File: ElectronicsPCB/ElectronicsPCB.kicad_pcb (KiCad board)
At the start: 4 copper layers, 15 parts

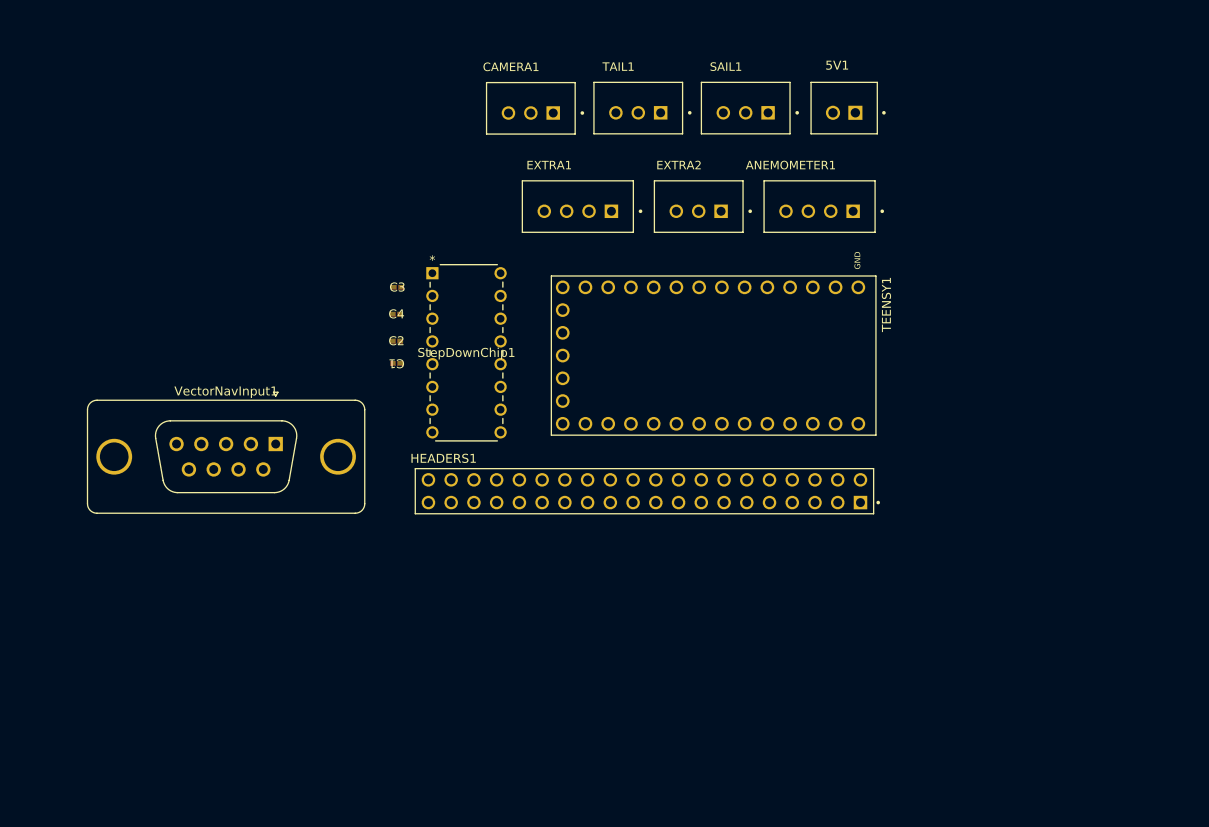
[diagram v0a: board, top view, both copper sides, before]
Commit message: added xbee footprint & xbee to layout
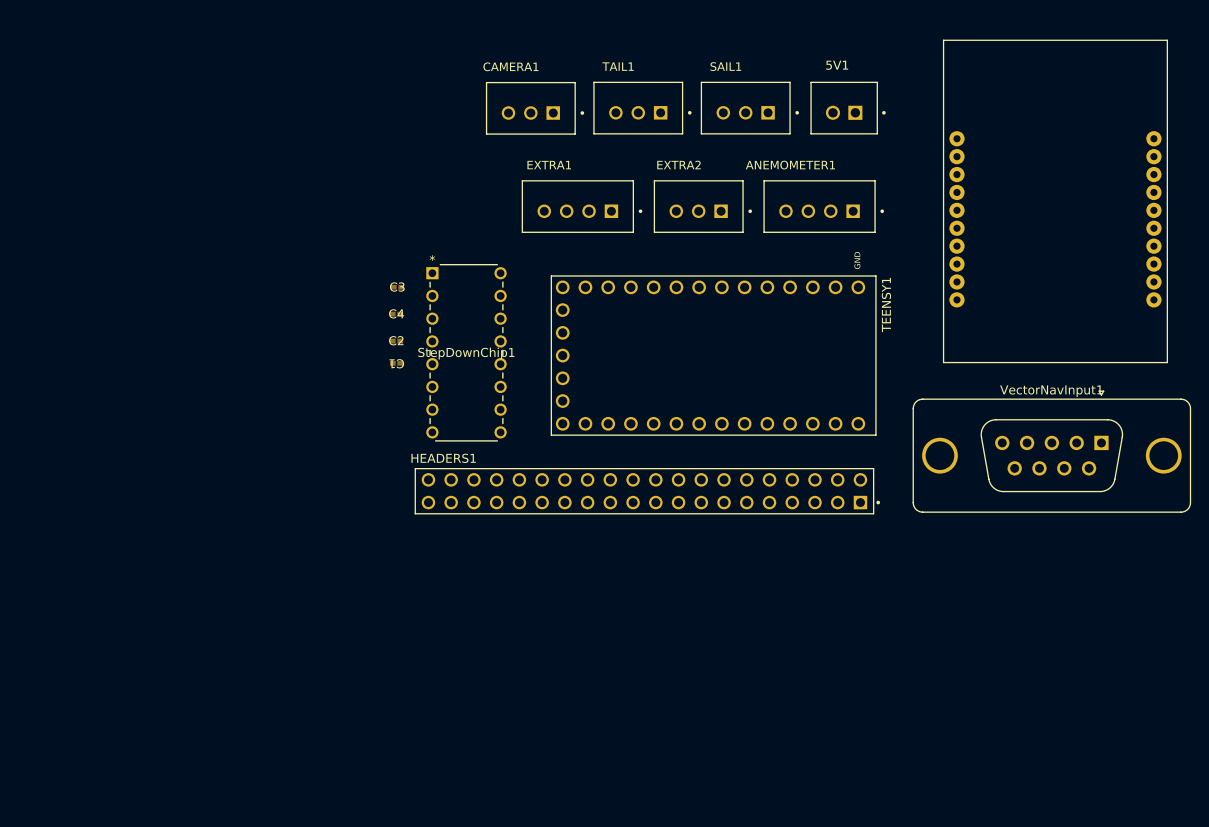
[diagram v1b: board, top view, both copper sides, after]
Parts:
- added XBEE1: ~, ElectronicsFootprints:XBee, F.Cu at (211.6, 66.9)
- moved VectorNavInput1 92.2 mm to (214.2, 95.9)

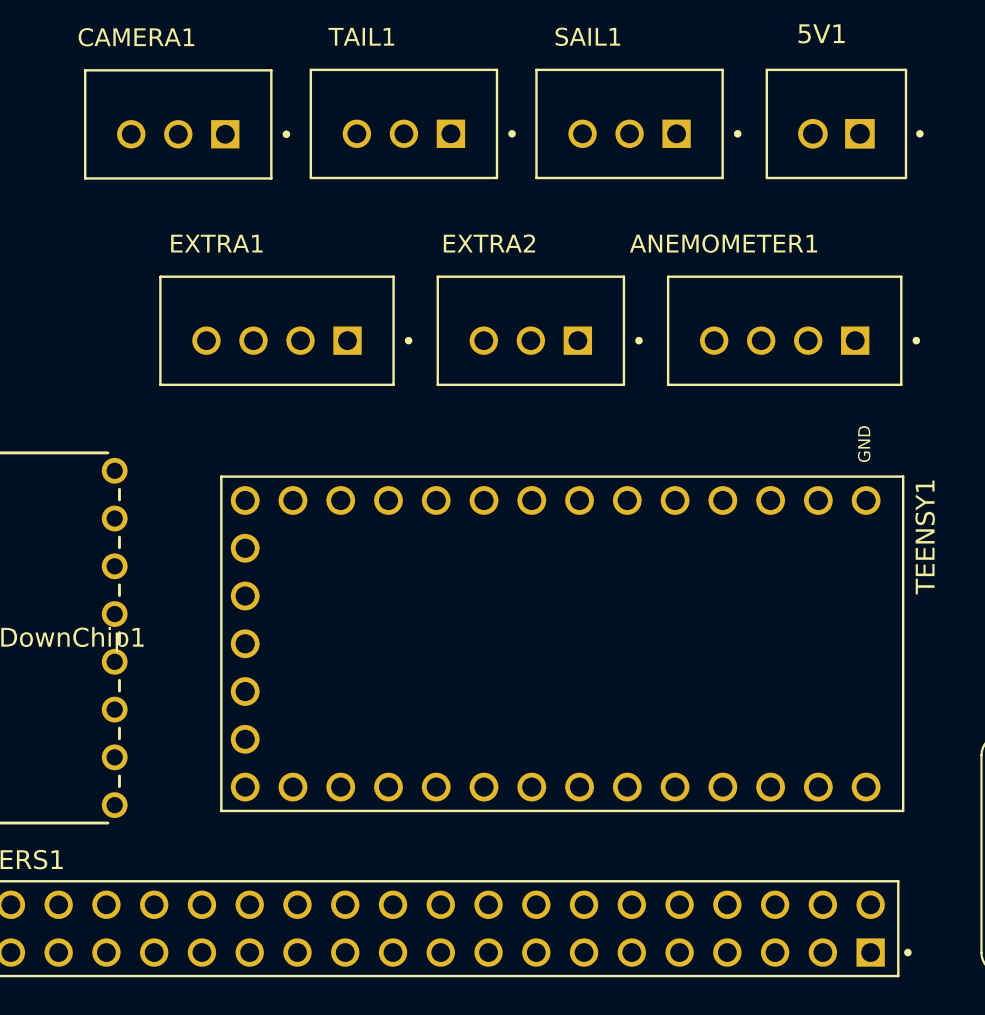
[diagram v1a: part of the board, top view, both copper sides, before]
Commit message: began adding traces to layout, updated connections on schematic
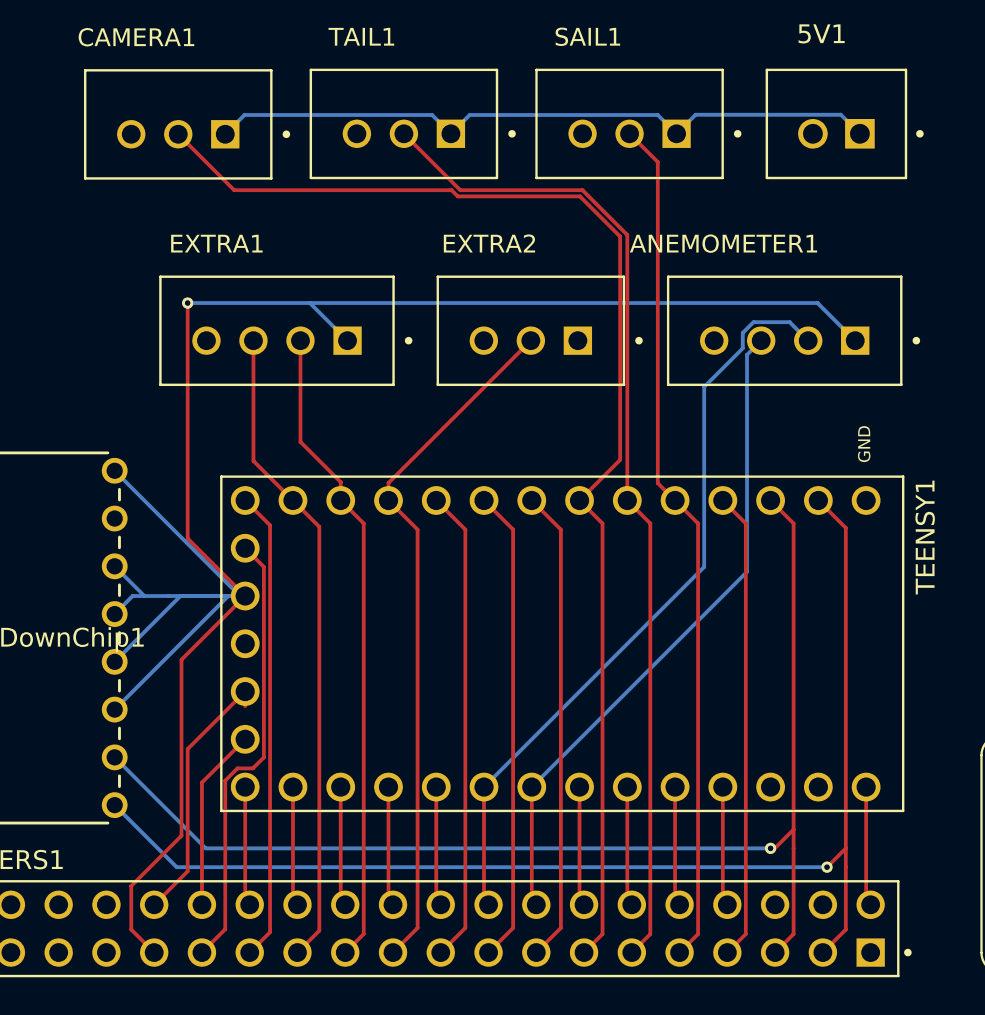
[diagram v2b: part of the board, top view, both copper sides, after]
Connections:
- HEADERS1 pad 15: 6 -> XBeeRESET
- HEADERS1 pad 17: 7 -> XBeeTX
- HEADERS1 pad 19: 8 -> XBeeRX
- HEADERS1 pad 21: 9 -> Extra3
- HEADERS1 pad 23: 10 -> Extra40
- HEADERS1 pad 25: 11 -> Extra41
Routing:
- net +3.3V: track 0.00 -> 115.6 mm, vias 0 -> 1
- net TeensyRX: track 0.00 -> 65.8 mm, vias 0 -> 1
- net Camera: track 0.00 -> 65.6 mm
- net TeensyTX: track 0.00 -> 63.5 mm, vias 0 -> 1
- net Tail: track 0.00 -> 53.2 mm
- net Sail: track 0.00 -> 45.5 mm
- net WindData0: track 0.00 -> 40.3 mm
- net Extra3: track 0.00 -> 36.9 mm
- net +5V: track 0.00 -> 36.3 mm
- net WindData1: track 0.00 -> 35.2 mm
- net Extra41: track 0.00 -> 34.5 mm
- net Extra40: track 0.00 -> 34.3 mm
- net XBeeRESET: track 0.00 -> 25.2 mm
- net XBeeTX: track 0.00 -> 25.2 mm
- net XBeeRX: track 0.00 -> 25.2 mm
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
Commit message: resolved all erc checker issues
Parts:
- moved XBEE1 95.8 mm to (118.2, 88.0), turned to 180 degrees
- moved VectorNavInput1 91.8 mm to (130.4, 58.4)
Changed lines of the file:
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@@
 	(footprint "ElectronicsFootprints:XBee"
 		(layer "F.Cu")
-		(at 211.6 66.9)
+		(at 118.2 88 180)
 		(property "Reference" "XBEE1"
-			(at 0 -0.5 0)
+			(at 0 -0.5 180)
 			(unlocked yes)
 			(layer "F.SilkS")
@@
 		)
 		(property "Value" "~"
-			(at 0 1 0)
+			(at 0 1 180)
 			(unlocked yes)
 			(layer "F.Fab")
@@
 		)
 		(property "Datasheet" ""
-			(at 0 0 0)
+			(at 0 0 180)
 			(unlocked yes)
 			(layer "F.Fab")
@@
 		)
 		(property "Description" ""
-			(at 0 0 0)
+			(at 0 0 180)
 			(unlocked yes)
 			(layer "F.Fab")
@@
 		(attr through_hole)
 		(fp_line
+			(start 10 20)
+			(end -15 20)
+			(stroke
+				(width 0.1)
+				(type default)
+			)
+			(layer "F.SilkS")
+		)
+		(fp_line
+			(start 10 -16)
+			(end 10 20)
+			(stroke
+				(width 0.1)
+				(type default)
+			)
+			(layer "F.SilkS")
+		)
+		(fp_line
+			(start -15 20)
+			(end -15 -16)
+			(stroke
+				(width 0.1)
+				(type default)
+			)
+			(layer "F.SilkS")
+		)
+		(fp_line
 			(start -15 -16)
 			(end 10 -16)
@@
 			(layer "F.SilkS")
 		)
-		(fp_line
-			(start -15 20)
-			(end -15 -16)
-			(stroke
-				(width 0.1)
-				(type default)
-			)
-			(layer "F.SilkS")
-		)
-		(fp_line
-			(start 10 -16)
-			(end 10 20)
-			(stroke
-				(width 0.1)
-				(type default)
-			)
-			(layer "F.SilkS")
-		)
-		(fp_line
-			(start 10 20)
-			(end -15 20)
-			(stroke
-				(width 0.1)
-				(type default)
-			)
-			(layer "F.SilkS")
-		)
 		(fp_text user "${REFERENCE}"
-			(at 0 -2 0)
+			(at 0 -2 180)
 			(unlocked yes)
 			(layer "F.Fab")
@@
 		)
 		(pad "1" thru_hole circle
-			(at -13.5 -5)
+			(at -13.5 -5 180)
 			(size 1.7 1.7)
 			(drill 0.8)
@@
 		)
 		(pad "2" thru_hole circle
-			(at -13.5 -3)
+			(at -13.5 -3 180)
 			(size 1.7 1.7)
 			(drill 0.8)
@@
 		)
 		(pad "3" thru_hole circle
-			(at -13.5 -1)
+			(at -13.5 -1 180)
 			(size 1.7 1.7)
 			(drill 0.8)
@@
 		)
 		(pad "4" thru_hole circle
-			(at -13.5 1)
+			(at -13.5 1 180)
 			(size 1.7 1.7)
 			(drill 0.8)
@@
 		)
 		(pad "5" thru_hole circle
-			(at -13.5 3)
+			(at -13.5 3 180)
 			(size 1.7 1.7)
 			(drill 0.8)
@@
 		)
 		(pad "6" thru_hole circle
-			(at -13.5 5)
+			(at -13.5 5 180)
 			(size 1.7 1.7)
 			(drill 0.8)
@@
 		)
 		(pad "7" thru_hole circle
-			(at -13.5 7)
+			(at -13.5 7 180)
 			(size 1.7 1.7)
 			(drill 0.8)
@@
 		)
 		(pad "8" thru_hole circle
-			(at -13.5 9)
+			(at -13.5 9 180)
 			(size 1.7 1.7)
 			(drill 0.8)
@@
 		)
 		(pad "9" thru_hole circle
-			(at -13.5 11)
+			(at -13.5 11 180)
 			(size 1.7 1.7)
 			(drill 0.8)
@@
 		)
 		(pad "10" thru_hole circle
-			(at -13.5 13)
+			(at -13.5 13 180)
 			(size 1.7 1.7)
 			(drill 0.8)
@@
 		)
 		(pad "11" thru_hole circle
-			(at 8.5 13)
+			(at 8.5 13 180)
 			(size 1.7 1.7)
 			(drill 0.8)
@@
 		)
 		(pad "12" thru_hole circle
-			(at 8.5 11)
+			(at 8.5 11 180)
 			(size 1.7 1.7)
 			(drill 0.8)
@@
 		)
 		(pad "13" thru_hole circle
-			(at 8.5 9)
+			(at 8.5 9 180)
 			(size 1.7 1.7)
 			(drill 0.8)
@@
 		)
 		(pad "14" thru_hole circle
-			(at 8.5 7)
+			(at 8.5 7 180)
 			(size 1.7 1.7)
 			(drill 0.8)
@@
 		)
 		(pad "15" thru_hole circle
-			(at 8.5 5)
+			(at 8.5 5 180)
 			(size 1.7 1.7)
 			(drill 0.8)
@@
 		)
 		(pad "16" thru_hole circle
-			(at 8.5 3)
+			(at 8.5 3 180)
 			(size 1.7 1.7)
 			(drill 0.8)
@@
 		)
 		(pad "17" thru_hole circle
-			(at 8.5 1)
+			(at 8.5 1 180)
 			(size 1.7 1.7)
 			(drill 0.8)
@@
 		)
 		(pad "18" thru_hole circle
-			(at 8.5 -1)
+			(at 8.5 -1 180)
 			(size 1.7 1.7)
 			(drill 0.8)
@@
 		)
 		(pad "19" thru_hole circle
-			(at 8.5 -3)
+			(at 8.5 -3 180)
 			(size 1.7 1.7)
 			(drill 0.8)
@@
 		)
 		(pad "20" thru_hole circle
-			(at 8.5 -5)
+			(at 8.5 -5 180)
 			(size 1.7 1.7)
 			(drill 0.8)
@@
 			(polygon
 				(pts
-					(xy 196.6 50.9) (xy 221.6 50.9) (xy 221.6 86.9) (xy 196.6 86.9)
+					(xy 133.2 104) (xy 108.2 104) (xy 108.2 68) (xy 133.2 68)
 				)
 			)
@@
 	(footprint "Connector_Dsub:DSUB-9_Socket_Vertical_P2.77x2.84mm_MountingHoles"
 		(layer "F.Cu")
-		(at 214.24 95.88)
+		(at 130.44 58.38)
 		(descr "9-pin D-Sub connector, straight/vertical, THT-mount, socket (female), pitch 2.77x2.84mm, distance of mounting holes 25mm, see https://disti-assets.s3.amazonaws.com/tonar/files/datasheets/16730.pdf")
 		(tags "9-pin D-Sub connector straight vertical THT socket pitch 2.77x2.84mm mounting holes distance 25mm")

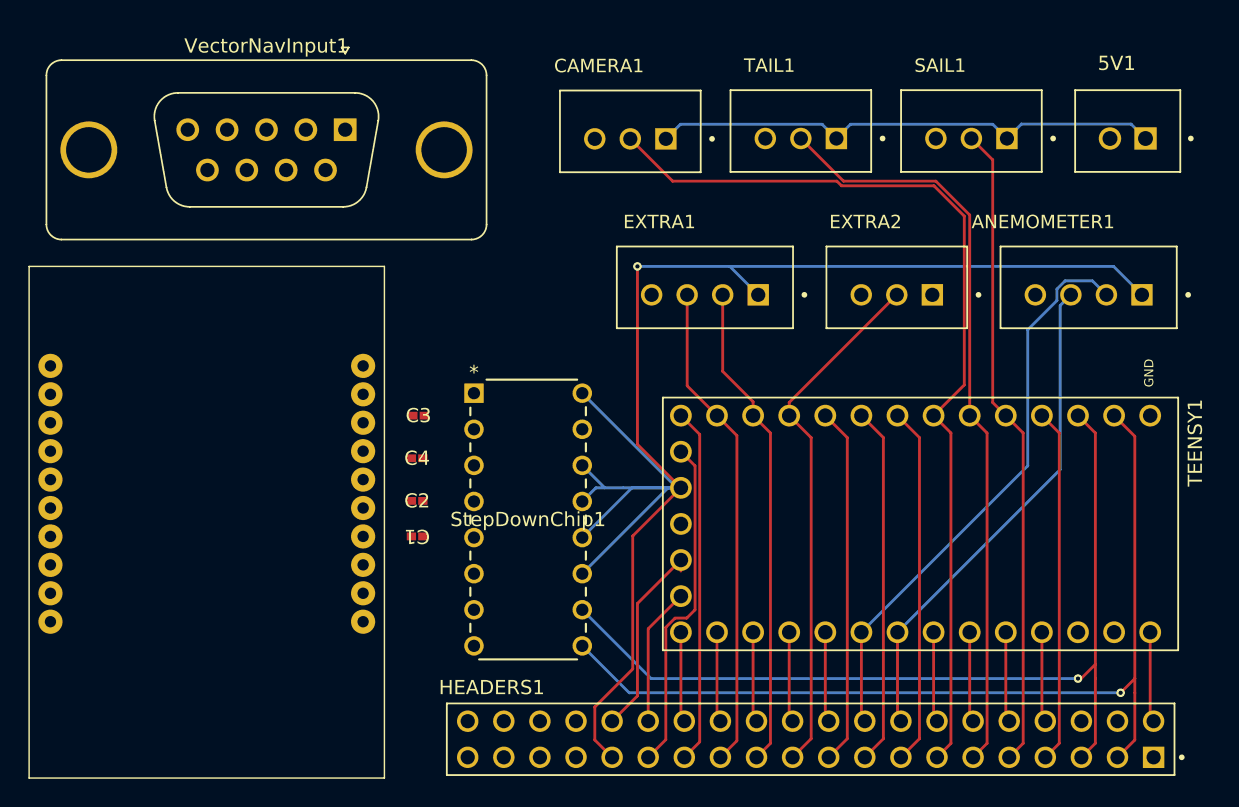
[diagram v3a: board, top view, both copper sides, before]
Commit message: changed layout and routed traces - look at v1 for most updated version
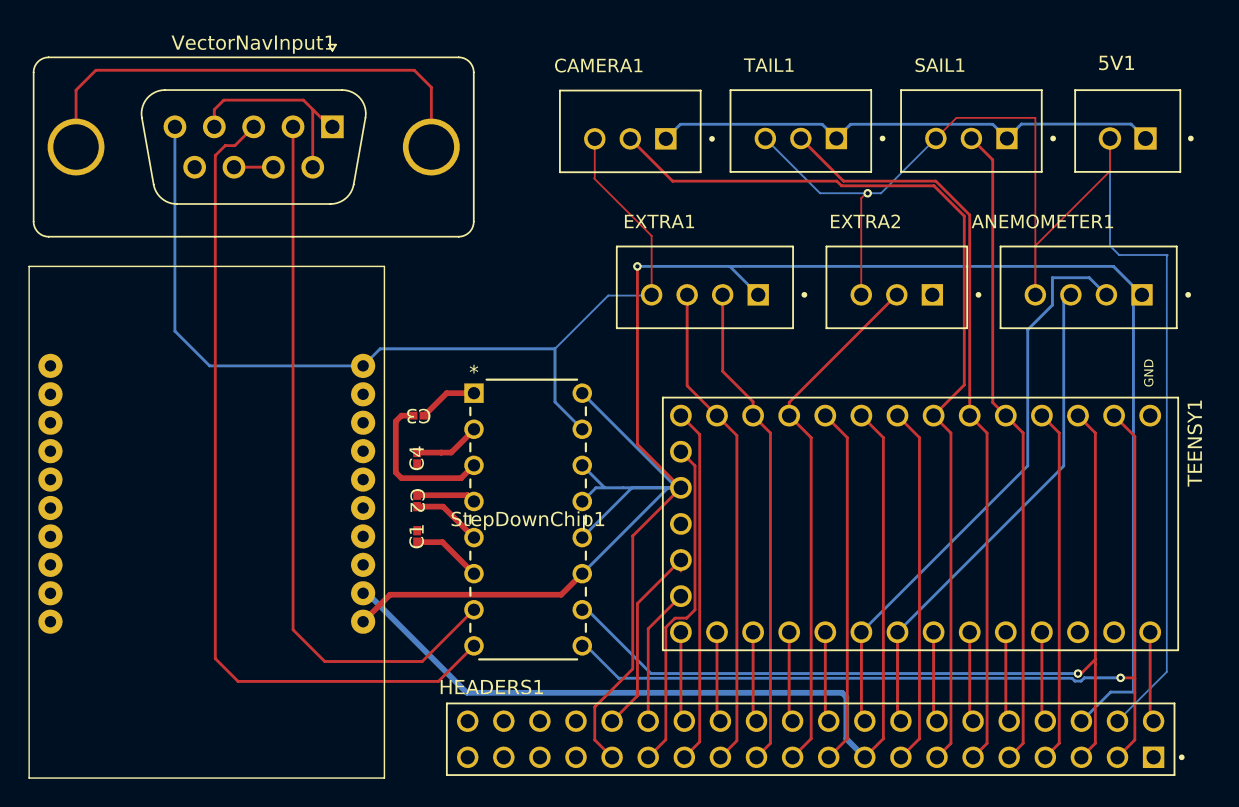
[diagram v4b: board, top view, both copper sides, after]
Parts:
- moved VectorNavInput1 0.92 mm to (129.5, 58.2)
- turned C1 to 90 degrees
- turned C2 to -90 degrees
- turned C3 to 180 degrees
- turned C4 to 90 degrees
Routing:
- net GND: track 0.00 -> 170.1 mm, vias 0 -> 1
- net VectorNavTX: track 0.00 -> 58.8 mm
- net VectorNavRX: track 0.00 -> 50.6 mm
- net +3.3V: track 115.6 -> 165.1 mm
- net XBeeTX: track 25.2 -> 67.0 mm
- net unconnected-(VectorNavInput1-PAD-Pad0): track 0.00 -> 34.3 mm
- net Net-(VectorNavInput1-Pad1): track 0.00 -> 14.6 mm
- net Net-(StepDownChip1-C1-): track 0.00 -> 11.0 mm
- net Net-(StepDownChip1-V-): track 0.00 -> 4.92 mm
- net Net-(StepDownChip1-C2-): track 0.00 -> 4.90 mm
- net Net-(StepDownChip1-V+): track 0.00 -> 4.71 mm
- net Net-(StepDownChip1-C2+): track 0.00 -> 4.18 mm
- net Net-(StepDownChip1-C1+): track 0.00 -> 4.15 mm
- net Net-(VectorNavInput1-Pad7): track 0.00 -> 2.77 mm
- net WindData0: track 40.3 -> 41.2 mm
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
